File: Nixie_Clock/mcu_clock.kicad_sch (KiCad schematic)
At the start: 0 parts

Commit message: Complete prelim nixie driver. Begin MCU work.
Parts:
- added U1: ESP32-WROOM-32E, RF_Module:ESP32-WROOM-32, symbol RF_Module:ESP32-WROOM-32
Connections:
- new net 0_CC_DRV: U1.36 (IO22)
- new net 1_CA_DRV: U1.25 (IO0)
- new net 1_CC_DRV: U1.14 (IO12)
- new net 2_CA_DRV: U1.35 (TXD0/IO1)
- new net 2_CC_DRV: U1.16 (IO13)
- new net 3_CA_DRV: U1.24 (IO2)
- new net 3_CC_DRV: U1.13 (IO14)
- new net 4_CA_DRV: U1.34 (RXD0/IO3)
- new net 4_CC_DRV: U1.23 (IO15)
- new net 5_CA_DRV: U1.26 (IO4)
- new net 5_CC_DRV: U1.27 (IO16)
- new net 6_CA_DRV: U1.29 (IO5)
- new net 6_CC_DRV: U1.28 (IO17)
- new net 7_CC_DRV: U1.30 (IO18)
- new net 8_CC_DRV: U1.31 (IO19)
- new net 9_CC_DRV: U1.33 (IO21)
- new net GND: U1.1 (GND), U1.15 (GND), U1.38 (GND), U1.39 (GND)
- new net LC_CC_DRV: U1.37 (IO23)
- new net RC_CC_DRV: U1.10 (IO25)
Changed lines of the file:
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@@
 (kicad_sch (version 20230121) (generator eeschema)
-  (paper "A4")
+  (paper "USLedger")
+  (wire (pts (xy 193.04 122.555) (xy 202.565 122.555))
+    (stroke (width 0) (type default))
+  )
+  (wire (pts (xy 193.04 120.015) (xy 202.565 120.015))
+    (stroke (width 0) (type default))
+  )
+  (wire (pts (xy 193.04 135.255) (xy 202.565 135.255))
+    (stroke (width 0) (type default))
+  )
+  (wire (pts (xy 193.04 127.635) (xy 202.565 127.635))
+    (stroke (width 0) (type default))
+  )
+  (wire (pts (xy 193.04 102.235) (xy 202.565 102.235))
+    (stroke (width 0) (type default))
+  )
+  (wire (pts (xy 193.04 97.155) (xy 202.565 97.155))
+    (stroke (width 0) (type default))
+  )
+  (wire (pts (xy 193.04 132.715) (xy 202.565 132.715))
+    (stroke (width 0) (type default))
+  )
+  (wire (pts (xy 193.04 109.855) (xy 202.565 109.855))
+    (stroke (width 0) (type default))
+  )
+  (wire (pts (xy 193.04 112.395) (xy 202.565 112.395))
+    (stroke (width 0) (type default))
+  )
+  (wire (pts (xy 193.04 94.615) (xy 202.565 94.615))
+    (stroke (width 0) (type default))
+  )
+  (wire (pts (xy 177.8 158.115) (xy 177.8 161.925))
+    (stroke (width 0) (type default))
+  )
+  (wire (pts (xy 193.04 130.175) (xy 202.565 130.175))
+    (stroke (width 0) (type default))
+  )
+  (wire (pts (xy 193.04 117.475) (xy 202.565 117.475))
+    (stroke (width 0) (type default))
+  )
+  (wire (pts (xy 193.04 125.095) (xy 202.565 125.095))
+    (stroke (width 0) (type default))
+  )
+  (wire (pts (xy 193.04 107.315) (xy 202.565 107.315))
+    (stroke (width 0) (type default))
+  )
+  (wire (pts (xy 193.04 92.075) (xy 202.565 92.075))
+    (stroke (width 0) (type default))
+  )
+  (wire (pts (xy 193.04 104.775) (xy 202.565 104.775))
+    (stroke (width 0) (type default))
+  )
+  (wire (pts (xy 193.04 99.695) (xy 202.565 99.695))
+    (stroke (width 0) (type default))
+  )
+  (wire (pts (xy 193.04 114.935) (xy 202.565 114.935))
+    (stroke (width 0) (type default))
+  )
+  (hierarchical_label "4_CA_DRV" (shape output) (at 202.565 99.695 0) (fields_autoplaced)
+    (effects (font (size 1.27 1.27)) (justify left))
+  )
+  (hierarchical_label "3_CA_DRV" (shape output) (at 202.565 97.155 0) (fields_autoplaced)
+    (effects (font (size 1.27 1.27)) (justify left))
+  )
+  (hierarchical_label "6_CC_DRV" (shape output) (at 202.565 120.015 0) (fields_autoplaced)
+    (effects (font (size 1.27 1.27)) (justify left))
+  )
+  (hierarchical_label "LC_CC_DRV" (shape output) (at 202.565 132.715 0) (fields_autoplaced)
+    (effects (font (size 1.27 1.27)) (justify left))
+  )
+  (hierarchical_label "7_CC_DRV" (shape output) (at 202.565 122.555 0) (fields_autoplaced)
+    (effects (font (size 1.27 1.27)) (justify left))
+  )
+  (hierarchical_label "5_CA_DRV" (shape output) (at 202.565 102.235 0) (fields_autoplaced)
+    (effects (font (size 1.27 1.27)) (justify left))
+  )
+  (hierarchical_label "6_CA_DRV" (shape output) (at 202.565 104.775 0) (fields_autoplaced)
+    (effects (font (size 1.27 1.27)) (justify left))
+  )
+  (hierarchical_label "1_CC_DRV" (shape output) (at 202.565 107.315 0) (fields_autoplaced)
+    (effects (font (size 1.27 1.27)) (justify left))
+  )
+  (hierarchical_label "2_CC_DRV" (shape output) (at 202.565 109.855 0) (fields_autoplaced)
+    (effects (font (size 1.27 1.27)) (justify left))
+  )
+  (hierarchical_label "1_CA_DRV" (shape output) (at 202.565 92.075 0) (fields_autoplaced)
+    (effects (font (size 1.27 1.27)) (justify left))
+  )
+  (hierarchical_label "4_CC_DRV" (shape output) (at 202.565 114.935 0) (fields_autoplaced)
+    (effects (font (size 1.27 1.27)) (justify left))
+  )
+  (hierarchical_label "9_CC_DRV" (shape output) (at 202.565 127.635 0) (fields_autoplaced)
+    (effects (font (size 1.27 1.27)) (justify left))
+  )
+  (hierarchical_label "RC_CC_DRV" (shape output) (at 202.565 135.255 0) (fields_autoplaced)
+    (effects (font (size 1.27 1.27)) (justify left))
+  )
+  (hierarchical_label "3_CC_DRV" (shape output) (at 202.565 112.395 0) (fields_autoplaced)
+    (effects (font (size 1.27 1.27)) (justify left))
+  )
+  (hierarchical_label "2_CA_DRV" (shape output) (at 202.565 94.615 0) (fields_autoplaced)
+    (effects (font (size 1.27 1.27)) (justify left))
+  )
+  (hierarchical_label "5_CC_DRV" (shape output) (at 202.565 117.475 0) (fields_autoplaced)
+    (effects (font (size 1.27 1.27)) (justify left))
+  )
+  (hierarchical_label "8_CC_DRV" (shape output) (at 202.565 125.095 0) (fields_autoplaced)
+    (effects (font (size 1.27 1.27)) (justify left))
+  )
+  (hierarchical_label "0_CC_DRV" (shape output) (at 202.565 130.175 0) (fields_autoplaced)
+    (effects (font (size 1.27 1.27)) (justify left))
+  )
+  (symbol (lib_id "power:GND") (at 177.8 161.925 0) (unit 1)
+    (in_bom yes) (on_board yes) (dnp no) (fields_autoplaced)
+    (property "Reference" "#PWR043" (at 177.8 168.275 0)
+      (effects (font (size 1.27 1.27)) hide)
+    )
+    (property "Value" "GND" (at 177.8 167.005 0)
+      (effects (font (size 1.27 1.27)))
+    )
+    (property "Footprint" "" (at 177.8 161.925 0)
+      (effects (font (size 1.27 1.27)) hide)
+    )
+    (property "Datasheet" "" (at 177.8 161.925 0)
+      (effects (font (size 1.27 1.27)) hide)
+    )
+    (pin "1")
+    (instances
+      (project "Nixie_Clock"
+        (path "/3ed0a7a2-efbd-4fe1-bc12-48e60b185ca7/dd785b04-b177-4b65-89fb-16bd08649dc7"
+          (reference "#PWR043") (unit 1)
+        )
+      )
+    )
+  )
+  (symbol (lib_id "RF_Module:ESP32-WROOM-32") (at 177.8 122.555 0) (unit 1)
+    (in_bom yes) (on_board yes) (dnp no) (fields_autoplaced)
+    (property "Reference" "U1" (at 179.9941 84.455 0)
+      (effects (font (size 1.27 1.27)) (justify left))
+    )
+    (property "Value" "ESP32-WROOM-32E" (at 179.9941 86.995 0)
+      (effects (font (size 1.27 1.27)) (justify left))
+    )
+    (property "Footprint" "RF_Module:ESP32-WROOM-32" (at 177.8 160.655 0)
+      (effects (font (size 1.27 1.27)) hide)
+    )
+    (property "Datasheet" "https://www.espressif.com/sites/default/files/documentation/esp32-wroom-32e_esp32-wroom-32ue_datasheet_en.pdf" (at 170.18 121.285 0)
+      (effects (font (size 1.27 1.27)) hide)
+    )
+    (pin "39")
+    (pin "37")
+    (pin "15")
+    (pin "29")
+    (pin "35")
+    (pin "6")
+    (pin "22")
+    (pin "14")
+    (pin "13")
+    (pin "33")
+    (pin "4")
+    (pin "1")
+    (pin "7")
+    (pin "36")
+    (pin "25")
+    (pin "20")
+    (pin "21")
+    (pin "3")
+    (pin "2")
+    (pin "38")
+    (pin "28")
+    (pin "12")
+    (pin "11")
+    (pin "24")
+    (pin "27")
+    (pin "9")
+    (pin "34")
+    (pin "8")
+    (pin "18")
+    (pin "16")
+    (pin "17")
+    (pin "26")
+    (pin "5")
+    (pin "10")
+    (pin "32")
+    (pin "30")
+    (pin "19")
+    (pin "23")
+    (pin "31")
+    (instances
+      (project "Nixie_Clock"
+        (path "/3ed0a7a2-efbd-4fe1-bc12-48e60b185ca7/dd785b04-b177-4b65-89fb-16bd08649dc7"
+          (reference "U1") (unit 1)
+        )
+      )
+    )
+  )
 )

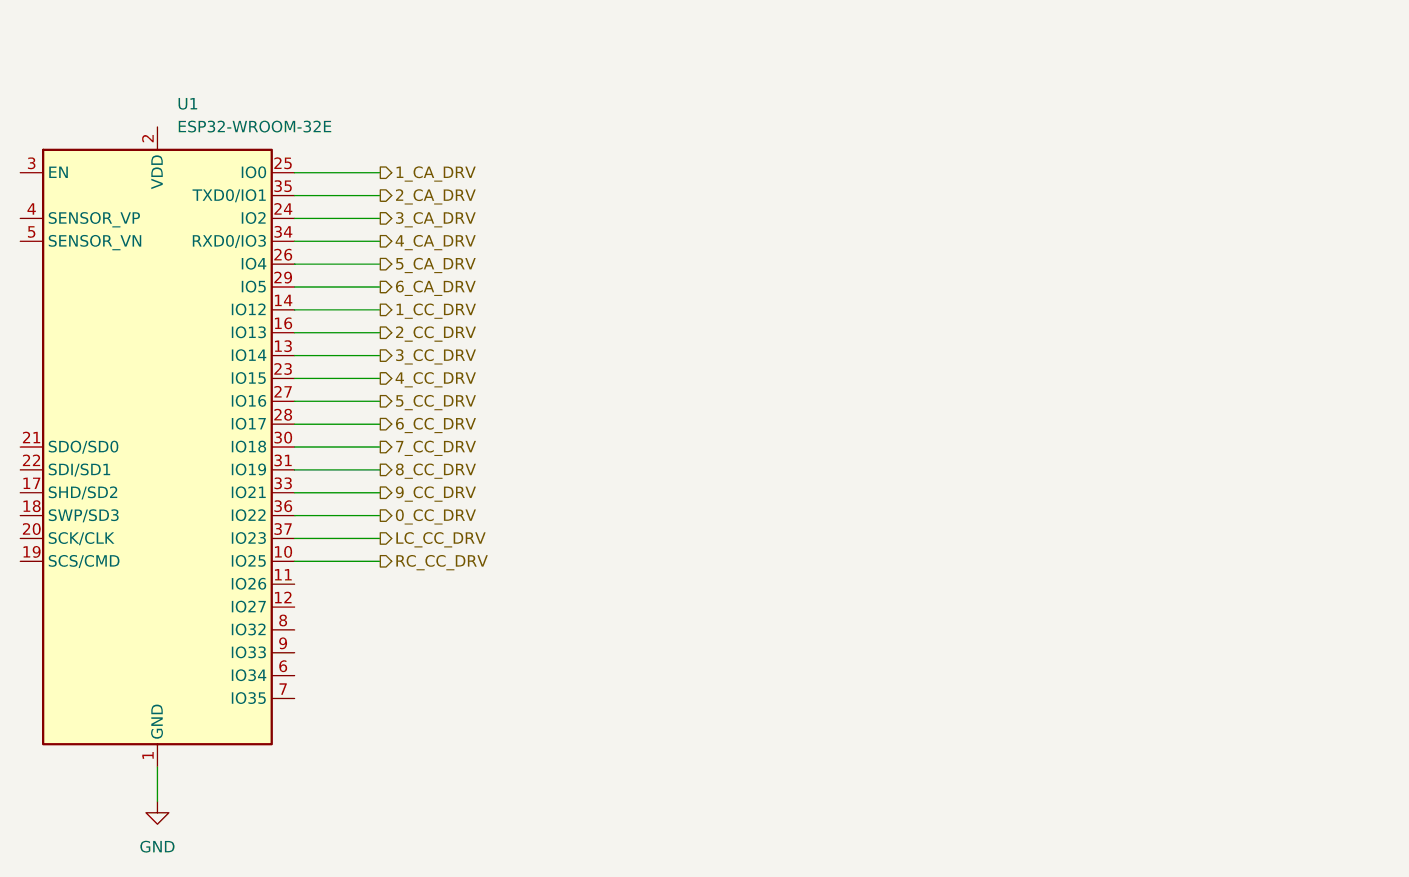
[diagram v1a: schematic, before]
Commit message: Add RTC, supercap, start work on supercap footprint
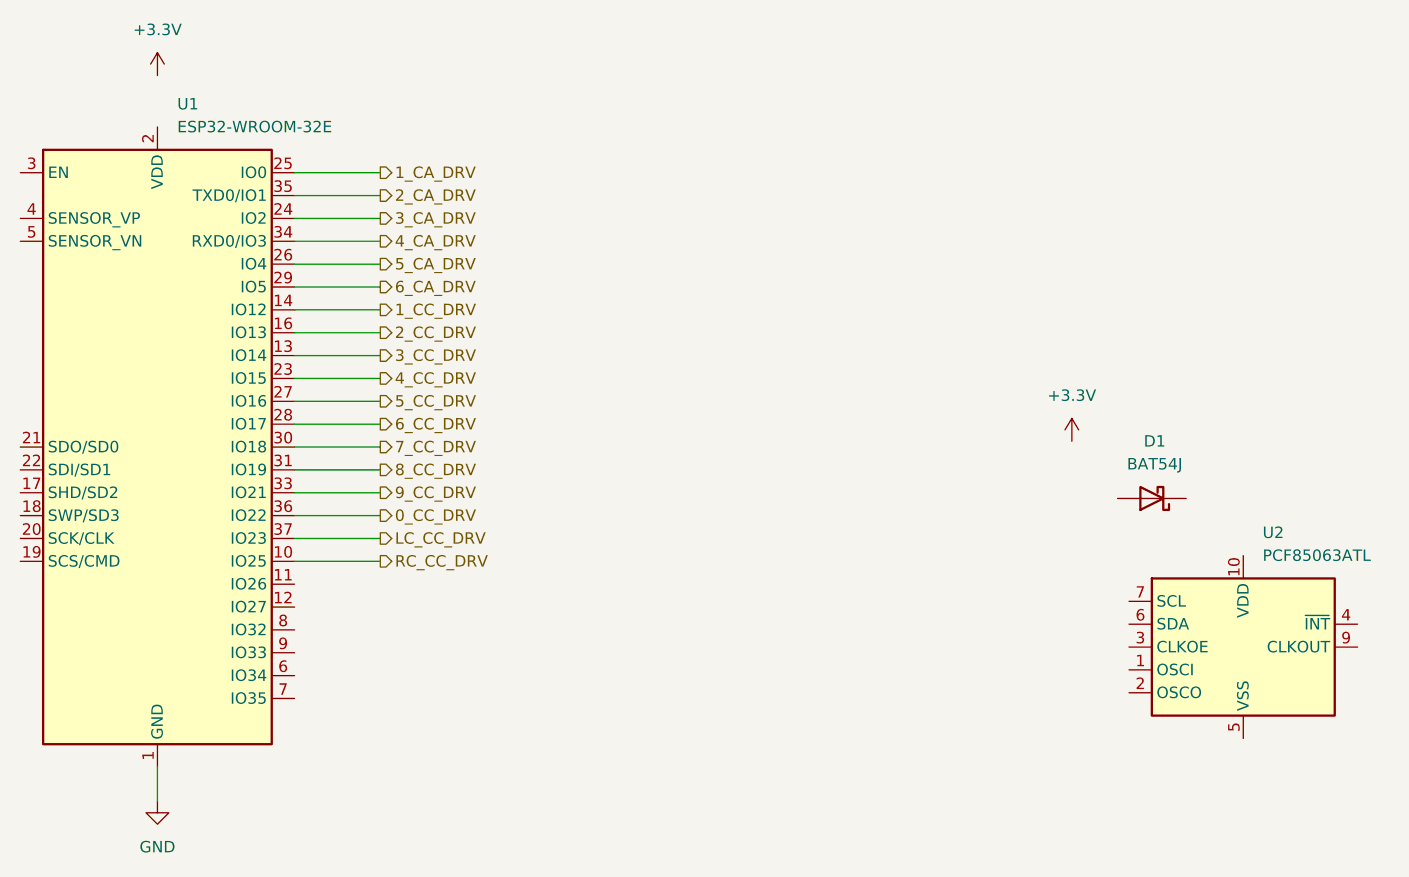
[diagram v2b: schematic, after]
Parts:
- added D1: BAT54J, Package_TO_SOT_SMD:SOT-323_SC-70, symbol Diode:BAT54J
- added U2: PCF85063ATL, Package_DFN_QFN:DFN-10-1EP_2.6x2.6mm_P0.5mm_EP1.3x2.2mm, symbol Timer_RTC:PCF85063ATL
- U1: MPN (none) -> 1965-ESP32-WROOM-32E-H4CT-ND; SPN (none) -> ESP32-WROOM-32E-H4
